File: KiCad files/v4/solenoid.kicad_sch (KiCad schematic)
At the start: 2 parts, among them J10 Conn_01x01_Socket, J11 Conn_01x01_Socket

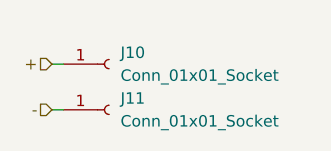
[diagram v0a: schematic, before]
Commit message: Fixed unconnected GND of MCU and flipped H-bridge sockets
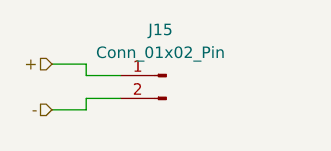
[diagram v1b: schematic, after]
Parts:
- removed J10, J11: Conn_01x01_Socket, Connector_PinSocket_2.54mm:PinSocket_1x01_P2.54mm_Vertical, symbol Connector:Conn_01x01_Socket
- added J15: Conn_01x02_Pin, Connector_PinHeader_2.54mm:PinHeader_1x02_P2.54mm_Vertical, symbol Connector:Conn_01x02_Pin
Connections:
- net +: now also J15.1 (Pin_1)
- net -: now also J15.2 (Pin_2)
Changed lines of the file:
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@@
 	(wire
 		(pts
-			(xy 140.97 95.25) (xy 142.24 95.25)
+			(xy 140.97 95.25) (xy 144.78 95.25)
 		)
 		(stroke
@@
 	(wire
 		(pts
-			(xy 140.97 100.33) (xy 142.24 100.33)
+			(xy 148.59 96.52) (xy 144.78 96.52)
+		)
+		(stroke
+			(width 0)
+			(type default)
+		)
+	)
+	(wire
+		(pts
+			(xy 144.78 99.06) (xy 148.59 99.06)
+		)
+		(stroke
+			(width 0)
+			(type default)
+		)
+	)
+	(wire
+		(pts
+			(xy 144.78 96.52) (xy 144.78 95.25)
+		)
+		(stroke
+			(width 0)
+			(type default)
+		)
+	)
+	(wire
+		(pts
+			(xy 140.97 100.33) (xy 144.78 100.33)
+		)
+		(stroke
+			(width 0)
+			(type default)
+		)
+	)
+	(wire
+		(pts
+			(xy 144.78 100.33) (xy 144.78 99.06)
 		)
 		(stroke
@@
 	)
 	(symbol
-		(lib_id "Connector:Conn_01x01_Socket")
-		(at 147.32 95.25 0)
+		(lib_id "Connector:Conn_01x02_Pin")
+		(at 153.67 96.52 0)
+		(mirror y)
 		(unit 1)
 		(exclude_from_sim no)
@@
 		(on_board yes)
 		(dnp no)
-		(fields_autoplaced yes)
-		(property "Reference" "J10"
-			(at 148.59 93.9799 0)
+		(property "Reference" "J15"
+			(at 153.035 91.44 0)
 			(effects
 				(font
 					(size 1.27 1.27)
 				)
-				(justify left)
 			)
 		)
-		(property "Value" "Conn_01x01_Socket"
-			(at 148.59 96.5199 0)
+		(property "Value" "Conn_01x02_Pin"
+			(at 153.035 93.98 0)
 			(effects
 				(font
 					(size 1.27 1.27)
 				)
-				(justify left)
 			)
 		)
-		(property "Footprint" "Connector_PinSocket_2.54mm:PinSocket_1x01_P2.54mm_Vertical"
-			(at 147.32 95.25 0)
+		(property "Footprint" "Connector_PinHeader_2.54mm:PinHeader_1x02_P2.54mm_Vertical"
+			(at 153.67 96.52 0)
 			(effects
 				(font
@@
 		)
 		(property "Datasheet" "~"
-			(at 147.32 95.25 0)
+			(at 153.67 96.52 0)
 			(effects
 				(font
@@
 			)
 		)
-		(property "Description" "Generic connector, single row, 01x01, script generated"
-			(at 147.32 95.25 0)
+		(property "Description" "Generic connector, single row, 01x02, script generated"
+			(at 153.67 96.52 0)
 			(effects
 				(font
@@
 		(pin "1"
 		)
+		(pin "2"
+		)
 		(instances
-			(project "NDE"
+			(project ""
 				(path "/6d7602eb-73a0-43e5-bb95-aef89688bbbb/39c62bc8-351f-46dc-9475-6ee4aea4f77d"
-					(reference "J10")
+					(reference "J15")
 					(unit 1)
 				)
 				(path "/6d7602eb-73a0-43e5-bb95-aef89688bbbb/fe62fdc0-f000-40f8-b2f1-51c831690bee"
-					(reference "J12")
+					(reference "J16")
 					(unit 1)
 				)
-			)
-		)
-	)
-	(symbol
-		(lib_id "Connector:Conn_01x01_Socket")
-		(at 147.32 100.33 0)
-		(unit 1)
-		(exclude_from_sim no)
-		(in_bom yes)
-		(on_board yes)
-		(dnp no)
-		(fields_autoplaced yes)
-		(property "Reference" "J11"
-			(at 148.59 99.0599 0)
-			(effects
-				(font
-					(size 1.27 1.27)
-				)
-				(justify left)
-			)
-		)
-		(property "Value" "Conn_01x01_Socket"
-			(at 148.59 101.5999 0)
-			(effects
-				(font
-					(size 1.27 1.27)
-				)
-				(justify left)
-			)
-		)
-		(property "Footprint" "Connector_PinSocket_2.54mm:PinSocket_1x01_P2.54mm_Vertical"
-			(at 147.32 100.33 0)
-			(effects
-				(font
-					(size 1.27 1.27)
-				)
-				(hide yes)
-			)
-		)
-		(property "Datasheet" "~"
-			(at 147.32 100.33 0)
-			(effects
-				(font
-					(size 1.27 1.27)
-				)
-				(hide yes)
-			)
-		)
-		(property "Description" "Generic connector, single row, 01x01, script generated"
-			(at 147.32 100.33 0)
-			(effects
-				(font
-					(size 1.27 1.27)
-				)
-				(hide yes)
-			)
-		)
-		(pin "1"
-		)
-		(instances
-			(project "NDE"
-				(path "/6d7602eb-73a0-43e5-bb95-aef89688bbbb/39c62bc8-351f-46dc-9475-6ee4aea4f77d"
-					(reference "J11")
-					(unit 1)
-				)
-				(path "/6d7602eb-73a0-43e5-bb95-aef89688bbbb/fe62fdc0-f000-40f8-b2f1-51c831690bee"
-					(reference "J13")
-					(unit 1)
-				)
